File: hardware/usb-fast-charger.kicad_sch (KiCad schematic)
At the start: 38 parts, among them J3 USB_C_Receptacle_USB2.0_16P, J4 BAT, J6 ON, J7 ON, SW1 SW_Reed, U7 MAX77751CEFG+, U8 LPV521, U9 MAX4906ELB+T

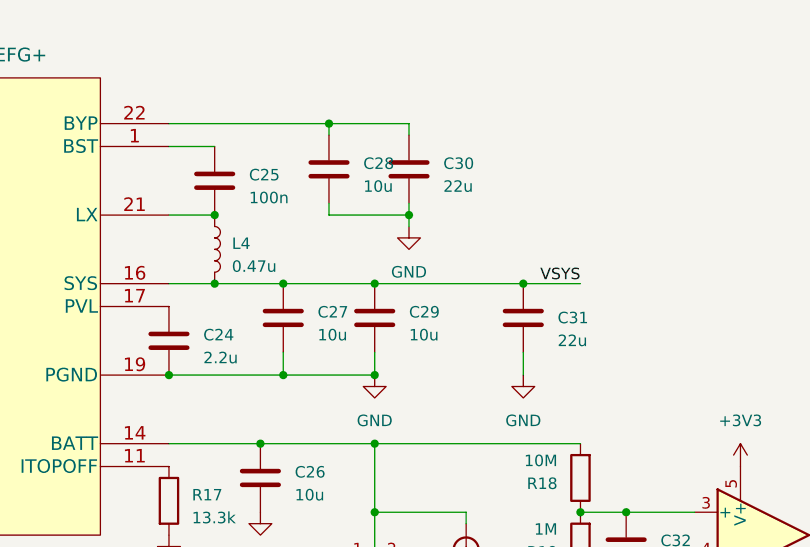
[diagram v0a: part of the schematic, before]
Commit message: add nix flake and initial esp32-c6 project structure with probe-rs and defmt
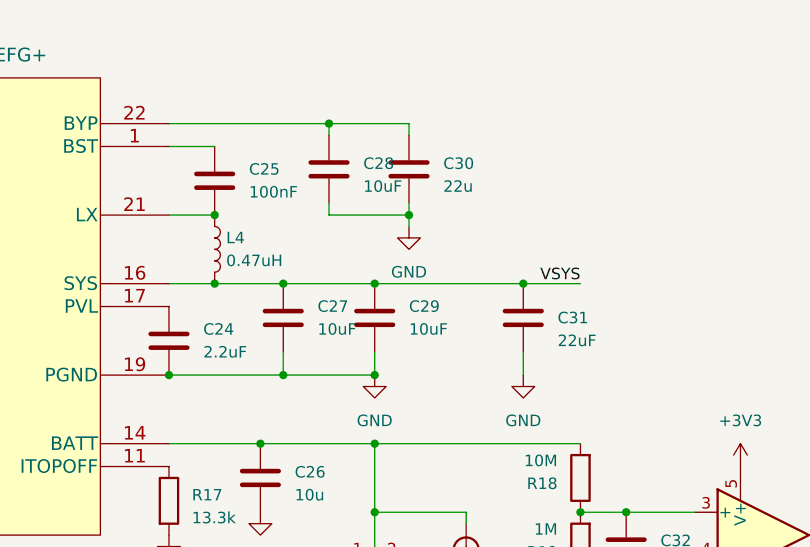
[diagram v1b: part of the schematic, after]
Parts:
- C24: value 2.2u -> 2.2uF
- C25: value 100n -> 100nF
- C27, C28, C29: value 10u -> 10uF
- C31: value 22u -> 22uF
- J3: LCSC Part # (none) -> C2843970
- L4: value 0.47u -> 0.47uH
- SW1: LCSC Part # (none) -> C315909
- U7: LCSC Part # (none) -> C2908590
- U8: LCSC Part # (none) -> C779403
- U9: LCSC Part # (none) -> C2150885
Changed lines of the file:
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@@
 			)
 		)
+		(property "LCSC Part #" "C779403"
+			(at 231.14 95.25 0)
+			(effects
+				(font
+					(size 1.27 1.27)
+				)
+				(hide yes)
+			)
+		)
 		(pin "4"
 		)
@@
 			)
 		)
-		(property "Value" "22u"
+		(property "Value" "22uF"
 			(at 208.28 73.66 0)
 			(effects
@@
 			)
 		)
-		(property "Value" "10u"
+		(property "Value" "10uF"
 			(at 186.69 56.515 0)
 			(effects
@@
 			)
 		)
+		(property "LCSC Part #" "C315909"
+			(at 198.12 99.06 90)
+			(effects
+				(font
+					(size 1.27 1.27)
+				)
+				(hide yes)
+			)
+		)
 		(pin "1"
 		)
@@
 			)
 		)
+		(property "LCSC Part #" "C2908590"
+			(at 142.24 69.85 0)
+			(effects
+				(font
+					(size 1.27 1.27)
+				)
+				(hide yes)
+			)
+		)
 		(pin "20"
 		)
@@
 		(fields_autoplaced yes)
 		(property "Reference" "C24"
-			(at 168.91 73.025 0)
+			(at 168.91 72.3899 0)
 			(effects
 				(font
@@
 			)
 		)
-		(property "Value" "2.2u"
-			(at 168.91 75.565 0)
+		(property "Value" "2.2uF"
+			(at 168.91 74.9299 0)
 			(effects
 				(font
@@
 			)
 		)
+		(property "LCSC Part #" "C2150885"
+			(at 100.33 125.73 0)
+			(effects
+				(font
+					(size 1.27 1.27)
+				)
+				(hide yes)
+			)
+		)
 		(pin "9"
 		)
@@
 			)
 		)
+		(property "LCSC Part #" "C2843970"
+			(at 69.85 64.77 0)
+			(effects
+				(font
+					(size 1.27 1.27)
+				)
+				(hide yes)
+			)
+		)
 		(pin "S1"
 		)
@@
 		(fields_autoplaced yes)
 		(property "Reference" "C29"
-			(at 191.77 70.485 0)
+			(at 191.77 69.8499 0)
 			(effects
 				(font
@@
 			)
 		)
-		(property "Value" "10u"
-			(at 191.77 73.025 0)
+		(property "Value" "10uF"
+			(at 191.77 72.3899 0)
 			(effects
 				(font
@@
 		(fields_autoplaced yes)
 		(property "Reference" "L4"
-			(at 172.085 62.865 0)
+			(at 171.45 62.2299 0)
 			(effects
 				(font
@@
 			)
 		)
-		(property "Value" "0.47u"
-			(at 172.085 65.405 0)
+		(property "Value" "0.47uH"
+			(at 171.45 64.7699 0)
 			(effects
 				(font
@@
 		(fields_autoplaced yes)
 		(property "Reference" "C25"
-			(at 173.99 55.245 0)
+			(at 173.99 54.6099 0)
 			(effects
 				(font
@@
 			)
 		)
-		(property "Value" "100n"
-			(at 173.99 57.785 0)
+		(property "Value" "100nF"
+			(at 173.99 57.1499 0)
 			(effects
 				(font
@@
 		(fields_autoplaced yes)
 		(property "Reference" "C27"
-			(at 181.61 70.485 0)
+			(at 181.61 69.8499 0)
 			(effects
 				(font
@@
 			)
 		)
-		(property "Value" "10u"
-			(at 181.61 73.025 0)
+		(property "Value" "10uF"
+			(at 181.61 72.3899 0)
 			(effects
 				(font
